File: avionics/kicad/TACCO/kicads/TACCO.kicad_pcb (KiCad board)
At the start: 6 copper layers, 55 x 35 mm, 143 parts, among them X2Y-CAN 4.7nF X2Y, X2Y-RS485 4.7nF X2Y

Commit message: feat(avionics): Phase 3 — TACCO HI-1573+PRU -> HI-6138 (MIL-STD-1553C)
gen_tacco_sch.py drift fixed first (pre-rename XO lib nickname/sym path,
stale TPS63031 datasheet text); regenerated output proven netlist-
identical to the committed schematic (0 comp / 0 pin-net diffs), ERC 0.
Then: 1553-XCVR -> HI-6138PCIF, X-50M/C-50M/R-1553IRQ/C-1553D, PB2
P1-7/8/9 -> M1553B_IRQN/MRN/TX_INH, P1-20 -> SPI0_B_CS_1553. TACCO's
_B_ net suffix kept (cape-B convention, not a 1553B label).

PCB patched in place. HI-6138 at the old site (142.86, 111.49, B.Cu).
No collision-free site within 20 mm on either side for the 4 new parts
(TACCO area crisis) -> parked off-board, owner placement item in WBS.
swap tool: NPTH now blocks the opposite side; courtyard margin 0.25 mm.

Gates: ERC 0; DRC 169 = pre-change baseline 169 (no new violations),
0 schematic parity; unconnected 480 -> 482.

Co-Authored-By: Claude Opus 5.5 <noreply@anthropic.com>
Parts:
- removed the 1553-XCVR at (142.9, 111.5)
- added 1553-XCVR: HI-6138PCIF, Serenity-Custom:Holt_HI-6138_QFN-48_6x6mm_P0.4mm_EP4.6mm, B.Cu at (142.9, 111.5)
- added C-1553D: 100nF, Capacitor_SMD:C_0402_1005Metric, B.Cu at (184.0, 92.5)
- added C-50M: 100nF, Capacitor_SMD:C_0402_1005Metric, B.Cu at (180.0, 92.5)
- added R-1553IRQ: 10k, Resistor_SMD:R_0402_1005Metric, B.Cu at (188.0, 92.5)
- added X-50M: 50MHz 3.3V, Oscillator:Oscillator_SMD_ECS_2520MV-xxx-xx-4Pin_2.5x2.0mm, B.Cu at (192.0, 92.5)
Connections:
- PB2-P1 pad 10: PRU_1553B_TX_P -> (no net)
- PB2-P1 pad 20: M1553B_TX_INH -> SPI0_B_CS_1553
- PB2-P1 pad 7: PRU_1553B_RX_N -> M1553B_IRQN
- PB2-P1 pad 8: PRU_1553B_RX_P -> M1553B_MRN
- PB2-P1 pad 9: PRU_1553B_TX_N -> M1553B_TX_INH

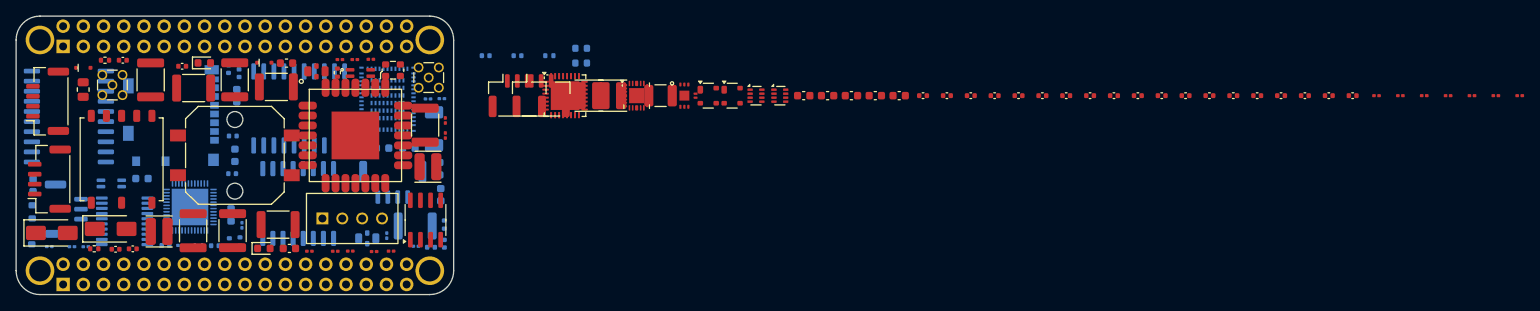
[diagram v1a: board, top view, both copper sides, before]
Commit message: feat(avionics): TACCO Rev S3 — area recovery, bare STM32WLE5JC mLRS radio, verified PB2 header map, DRC-clean placement
Owner decisions of 2026-09-29 (avionics/WBS.md §1.2a "TACCO area recovery"),
documented first per the design-shift gate, then implemented:

- Ferrite-bead spec defect: FB-SDIO1..6 / FB-WIOE5-1/2 carried Würth 742792510,
  which wurth-742792510.pdf shows is the 1812 5 A / 70 Ω power bead; the signal
  beads are now 0402 600 Ω positions (MPN owner-select). FB1 keeps 742792510.
- Boot/bind switch PTS125 -> C&K KMR2; SWD header JST-GH -> Tag-Connect
  TC2030-NL pads. Wi-Fi/TPM 100 nF bypasses -> 0201 (rail-cell sites).
- Seeed Wio-E5 (Chinese-built module) -> bare ST STM32WLE5JCU6 with Epson
  TG2520SMN 32 MHz TCXO and pSemi PE4259 antenna switch; pins from DS13105 Rev 9
  Fig. 9 / Table 19; SMPS Lout 15 µH / Cout 470 nF per DS13105; TCXO series 10 pF
  per Table 58. RF matching values are tagged VERIFY AN5457 (not obtainable here).
- PB2 P1/P2 header map rebuilt from the owner-supplied PocketBeagle 2 schematic
  (REF-SENSOR-021, avionics/kicad/PB2_HEADER_PINMAP.md): the Rev S2 map put GND on
  the PB2's 5 V VIN pin and peripherals on the wrong balls. MCAN0 on P2-5/7,
  UART2 = RS-485 with hardware DE, UART0 = mLRS, UART1 = BT, SPI0 + CS1, RMII2 +
  MDIO0 for Ethernet (RMII0_* -> RMII2_*), EHRPWM2_A = fan.
- MMC2/SDIO is not on the PB2 headers: Type 2EL WLAN cannot be hosted; SDIO beads
  deleted, module SDIO pins NC. Owner decision: Wi-Fi moves to a USB module on
  USB1 (P1-9/11) — module selection is an open fab blocker.
- DP83825I pin table rebuilt from TI SNLS638C Table 4-1 (REF-SENSOR-020); the old
  table was not this part's pinout (Pilot shares the defect, not fixed here).
  Pin 2 (50MHzOut) now drives RMII2_REF_CLK.
- Non-stack-through rails (Commo Rev T standalone): the placer may use the
  top-face cells between rail pins for 0201 parts. The P2-3..10 gap idea was
  withdrawn once the real map showed P2-5/7 are the only MCAN0 pins.
- gen_tacco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
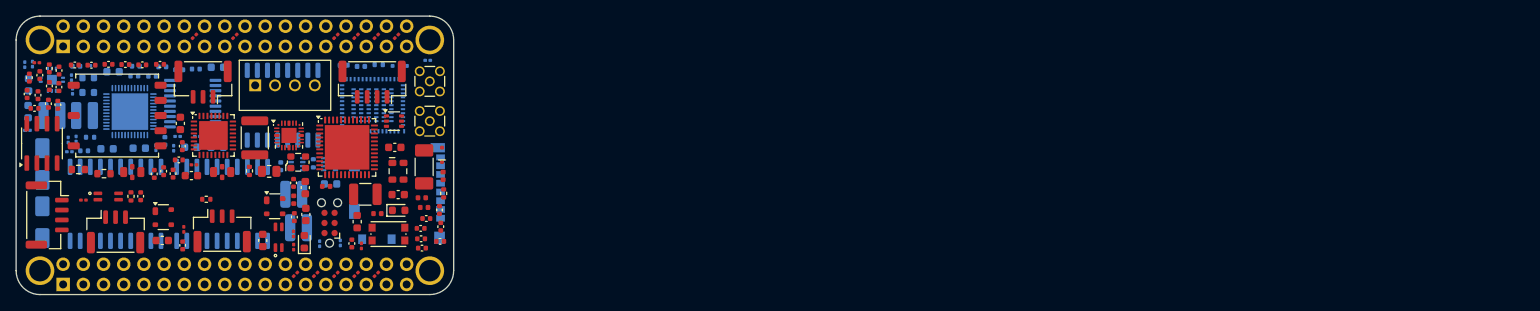
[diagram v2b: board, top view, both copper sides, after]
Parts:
- removed C-WIOE5-IN: 4.7uF, Capacitor_SMD:C_0603_1608Metric
- removed C-WIOE5-SH1, C-WIOE5-SH2: DNP, Capacitor_SMD:C_0201_0603Metric
- removed the C-ZB-SDVIO at (286.0, 97.5)
- removed the C-ZB-VIO at (289.0, 97.5)
- removed D-ANT-WIOE5: RCLAMP0502B, Serenity-Custom:RCLAMP0502B_SOD882
- removed FB-SDIO1, FB-SDIO2, FB-SDIO3, FB-SDIO4, FB-SDIO5, FB-SDIO6, FB-WIOE5-1, FB-WIOE5-2: 742792510, Inductor_SMD:L_1812_4532Metric
- removed J-ANT-WIOE5: MMCX vertical, Connector_Coaxial:MMCX_Molex_73415-1471_Vertical
- removed J-WIOE5-SWD: SM04B-GHS-TB, Connector_JST:JST_GH_SM04B-GHS-TB_1x04-1MP_P1.25mm_Horizontal
- removed L-WIOE5-SER: 0R link, Resistor_SMD:R_0402_1005Metric
- removed LED-WIOE5-G: Green, LED_SMD:LED_0603_1608Metric
- removed LED-WIOE5-R: Red, LED_SMD:LED_0603_1608Metric
- removed R-WIOE5-LEDG, R-WIOE5-LEDR: 1k, Resistor_SMD:R_0201_0603Metric
- removed R-WIOE5-RST: 22k, Resistor_SMD:R_0201_0603Metric
- removed R-WIOE5-SWCLK, R-WIOE5-SWDIO: 22R, Resistor_SMD:R_0201_0603Metric
- removed SW-WIOE5-BOOT: PTS125Sx43, Button_Switch_SMD:SW_Push_1P1T_NO_CK_PTS125Sx43PSMTR
- removed WIOE5: Wio-E5, Serenity-Custom:Seeed_WioE5_QFN28
- added C-MLRS-BULK: 4.7uF, Capacitor_SMD:C_0603_1608Metric, F.Cu at (168.6, 104.0)
- added C-MLRS-HSE: 10pF C0G, Capacitor_SMD:C_0402_1005Metric, F.Cu at (171.9, 114.2)
- added C-MLRS-RST: 100nF, Capacitor_SMD:C_0402_1005Metric, F.Cu at (171.9, 115.5)
- added C-MLRS-RX1: VERIFY AN5457, Capacitor_SMD:C_0402_1005Metric, F.Cu at (174.4, 114.0)
- added C-MLRS-RXN: VERIFY AN5457, Capacitor_SMD:C_0402_1005Metric, F.Cu at (174.3, 115.8)
- added C-MLRS-RXP: VERIFY AN5457, Capacitor_SMD:C_0402_1005Metric, F.Cu at (172.0, 116.7)
- added C-MLRS-SH1: DNP, Capacitor_SMD:C_0201_0603Metric, F.Cu at (164.4, 116.4)
- added C-MLRS-SH2: DNP, Capacitor_SMD:C_0201_0603Metric, F.Cu at (155.9, 114.9)
- added C-MLRS-SMPS: 100nF, Capacitor_SMD:C_0402_1005Metric, F.Cu at (139.5, 107.0)
- added C-MLRS-TCXO: 100nF, Capacitor_SMD:C_0402_1005Metric, F.Cu at (141.5, 105.6)
- added C-MLRS-TX0: VERIFY AN5457, Capacitor_SMD:C_0402_1005Metric, F.Cu at (155.9, 108.5)
- added C-MLRS-TX1: VERIFY AN5457, Capacitor_SMD:C_0402_1005Metric, F.Cu at (138.4, 107.3)
- added C-MLRS-TX2: VERIFY AN5457, Capacitor_SMD:C_0402_1005Metric, F.Cu at (139.1, 93.6)
- added C-MLRS-VBAT: 100nF, Capacitor_SMD:C_0402_1005Metric, F.Cu at (136.9, 93.6)
- added C-MLRS-VDD1: 100nF, Capacitor_SMD:C_0402_1005Metric, F.Cu at (134.7, 93.6)
- added C-MLRS-VDD2: 100nF, Capacitor_SMD:C_0402_1005Metric, F.Cu at (132.6, 93.6)
- added C-MLRS-VDDA1: 100nF, Capacitor_SMD:C_0402_1005Metric, F.Cu at (130.5, 93.7)
- added C-MLRS-VDDA2: 1uF, Capacitor_SMD:C_0402_1005Metric, F.Cu at (128.4, 93.6)
- added C-MLRS-VDDPA1: 100nF, Capacitor_SMD:C_0402_1005Metric, F.Cu at (126.2, 98.6)
- added C-MLRS-VDDPA2: 4.7uF, Capacitor_SMD:C_0603_1608Metric, F.Cu at (169.0, 109.9)
- added C-MLRS-VDDRF: 100nF, Capacitor_SMD:C_0402_1005Metric, F.Cu at (126.4, 96.4)
- added C-MLRS-VFB: 470nF, Capacitor_SMD:C_0402_1005Metric, F.Cu at (126.4, 94.3)
- added C-MLRS-VRPA: 100nF VERIFY AN5457, Capacitor_SMD:C_0402_1005Metric, B.Cu at (141.5, 94.2)
- added C-ZB-SDVIO: 100nF 6.3V X5R, Capacitor_SMD:C_0201_0603Metric, B.Cu at (127.5, 103.1)
- added C-ZB-VIO: 100nF 6.3V X5R, Capacitor_SMD:C_0201_0603Metric, F.Cu at (166.3, 90.0)
- added D-ANT-MLRS: RCLAMP0502B, Serenity-Custom:RCLAMP0502B_SOD882, F.Cu at (174.5, 104.9)
- added FB-MLRS-1: 600R@100MHz 0402, Inductor_SMD:L_0402_1005Metric, F.Cu at (160.0, 108.9)
- added FB-MLRS-2: 600R@100MHz 0402, Inductor_SMD:L_0402_1005Metric, F.Cu at (155.9, 110.6)
- added J-ANT-MLRS: MMCX vertical, Connector_Coaxial:MMCX_Molex_73415-1471_Vertical, F.Cu at (173.0, 100.7)
- added J-MLRS-SWD: TC2030-IDC-NL pads, Connector:Tag-Connect_TC2030-IDC-NL_2x03_P1.27mm_Vertical, F.Cu at (160.4, 113.5)
- added L-MLRS-PA: VERIFY AN5457, Inductor_SMD:L_0402_1005Metric, F.Cu at (166.4, 112.3)
- added L-MLRS-RX1: VERIFY AN5457, Inductor_SMD:L_0402_1005Metric, B.Cu at (164.3, 93.8)
- added L-MLRS-RX2: VERIFY AN5457, Inductor_SMD:L_0402_1005Metric, F.Cu at (174.7, 107.6)
- added L-MLRS-SER: 0R link, Resistor_SMD:R_0402_1005Metric, F.Cu at (174.7, 109.8)
- added L-MLRS-SMPS: 15uH, Inductor_SMD:L_0603_1608Metric, F.Cu at (163.9, 113.3)
- added L-MLRS-TX1: VERIFY AN5457, Inductor_SMD:L_0402_1005Metric, F.Cu at (172.0, 110.3)
- added L-MLRS-TX2: VERIFY AN5457, Inductor_SMD:L_0402_1005Metric, F.Cu at (172.3, 111.6)
- added LED-MLRS-G: Green, LED_SMD:LED_0603_1608Metric, F.Cu at (169.1, 111.9)
- added LED-MLRS-R: Red, LED_SMD:LED_0603_1608Metric, F.Cu at (157.2, 115.9)
- added MLRS-MCU: STM32WLE5JCU6, Package_DFN_QFN:QFN-48-1EP_7x7mm_P0.5mm_EP5.6x5.6mm, F.Cu at (162.6, 104.0)
- added R-MLRS-BOOT0: 10k, Resistor_SMD:R_0201_0603Metric, F.Cu at (163.7, 120.0)
- added R-MLRS-LEDG: 1k, Resistor_SMD:R_0201_0603Metric, F.Cu at (161.2, 90.0)
- added R-MLRS-LEDR: 1k, Resistor_SMD:R_0201_0603Metric, F.Cu at (156.1, 120.0)
- added R-MLRS-RST: 22k, Resistor_SMD:R_0201_0603Metric, F.Cu at (166.3, 120.0)
- added R-MLRS-SWCLK: 22R, Resistor_SMD:R_0201_0603Metric, F.Cu at (163.7, 90.0)
- added R-MLRS-SWDIO: 22R, Resistor_SMD:R_0201_0603Metric, F.Cu at (168.8, 90.0)
- added RFSW-MLRS: PE4259, Package_TO_SOT_SMD:SOT-363_SC-70-6, F.Cu at (168.5, 100.7)
- added SW-MLRS: KMR2 tact, Button_Switch_SMD:SW_Push_1P1T_NO_CK_KMR2, F.Cu at (167.8, 114.9)
- added X-MLRS: TG2520SMN 32MHz 1.8V clipped-sine, Oscillator:Oscillator_SMD_SeikoEpson_TG2520SMN-xxx-xxxxxx-4Pin_2.5x2.0mm, F.Cu at (169.0, 107.0)
- C-1V8RF-IN, C-25M, C-3V3-HF, C-3V3-IN, C-3V3-O1, C-3V3-O2, C-BST, C-CAN1, C-PLD1, C-RF-IN2, C-RF-O2, C-SS, C-SS18, D-ANT-RADIO, L-1V8RF, L-3V3, L-ANT-SER, L-RF1, L-RF2, R-AD0, R-EN3, R-FB3H, R-FB3L, R-RBIAS, TVS-1553N, TVS-1553P, U-1V8RF, U-3V3, U-3V3RF: moved to B.Cu
- C-1V8RF-O1, C-1V8RF-O2, C-485-2, C-485-3, C-485-4, C-485-5, C-485-6, C-BS, C-BST18, C-CAN6, C-FLASH1, C-PHY-A2, CMC-RS485, J-485, J-ETH, R-1553N, R-1553P, R-BST, R-CANT, R-TPMCS, X2Y-RS485: moved to F.Cu
- C-TPM2, C-TPM3, C-ZB-18-2, C-ZB-33-1, C-ZB-33-2: value 100nF -> 100nF 6.3V X5R; footprint Capacitor_SMD:C_0402_1005Metric -> Capacitor_SMD:C_0201_0603Metric; moved to B.Cu
- C-TPM4, C-ZB-18-1: value 100nF -> 100nF 6.3V X5R; footprint Capacitor_SMD:C_0402_1005Metric -> Capacitor_SMD:C_0201_0603Metric
- moved R-FB3L 181.0 mm to (123.1, 93.5), turned to 90 degrees
- moved R-EN3 170.1 mm to (128.0, 95.2), turned to 90 degrees
- moved C-ZB-33-2 154.9 mm to (128.1, 96.9), turned to 90 degrees
- moved R-FB18L 153.0 mm to (158.7, 120.0), turned to 45 degrees
- moved C-ZB-33-1 151.6 mm to (128.5, 102.9), turned to 90 degrees
- moved C-SS18 151.3 mm to (143.8, 102.6)
- moved C-TPM4 150.4 mm to (123.6, 93.4)
- moved R-FB18H 147.5 mm to (161.2, 120.0), turned to 45 degrees
- moved C-ZB-18-2 146.4 mm to (130.7, 93.7)
- moved R-FB3H 143.1 mm to (159.2, 116.1), turned to 90 degrees
- moved C-TPM1 142.4 mm to (122.7, 95.2), turned to 90 degrees
- moved C-PHY-CTD2 133.6 mm to (122.4, 97.3), turned to 90 degrees
- moved C-RF-IN2 133.5 mm to (128.6, 93.8)
- moved C-SS 131.6 mm to (161.8, 116.0), turned to 90 degrees
- moved C-TPM3 130.4 mm to (140.8, 104.1), turned to 90 degrees
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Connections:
- ETH-PHY pad 1: RMII0_RXD0 -> RMII2_TX_EN
- ETH-PHY pad 10: GND -> ETHB_TXN
- ETH-PHY pad 11: (no net) -> ETHB_TXP
- ETH-PHY pad 12: PHY1_RSTN -> (no net)
- ETH-PHY pad 13: MDIO0 -> PHY_XI_25M
- ETH-PHY pad 14: MDC0 -> ETH-PHY_RBIAS
- ETH-PHY pad 15: PHY1_INTRN -> MDIO0
- ETH-PHY pad 16: GND -> MDC0
- ETH-PHY pad 17: ETHB_TXP -> RMII2_RXD1
- ETH-PHY pad 18: ETHB_TXN -> RMII2_RXD0
- ETH-PHY pad 2: RMII0_RXD1 -> RMII2_REF_CLK
- ETH-PHY pad 20: GND -> RMII2_CRS_DV
- ETH-PHY pad 21: ETHB_RXP -> GND
- ETH-PHY pad 22: ETHB_RXN -> RMII2_RX_ER
- ETH-PHY pad 23: +3V3 -> RMII2_TXD0
- ETH-PHY pad 24: ETH-PHY_RBIAS -> RMII2_TXD1
- ETH-PHY pad 3: RMII0_RX_ER -> PHY1_INTRN
- ETH-PHY pad 4: RMII0_CRS_DV -> (no net)
- ETH-PHY pad 5: RMII0_TX_EN -> PHY1_RSTN
- ETH-PHY pad 6: RMII0_TXD0 -> +3V3
- ETH-PHY pad 7: RMII0_TXD1 -> ETHB_RXN
- ETH-PHY pad 8: PHY_XI_25M -> ETHB_RXP
- ETH-PHY pad 9: (no net) -> GND
- PB2-P1 pad 1: GND -> +5V
- PB2-P1 pad 10: (no net) -> BT_UART_CTS
- PB2-P1 pad 11: RS485_B_DE -> (no net)
- PB2-P1 pad 12: RS485_B_RX -> BT_UART_RTS
- PB2-P1 pad 13: RS485_B_TX -> PLD_CLK
- PB2-P1 pad 14: CAN_B_STB -> +3V3_PB2
- PB2-P1 pad 15: MCAN0_B_RX -> GND
- PB2-P1 pad 16: MCAN0_B_TX -> GND
- PB2-P1 pad 17: SD_CD -> (no net)
- PB2-P1 pad 19: (no net) -> RMII2_RX_ER
- PB2-P1 pad 2: GND -> RMII2_TX_EN
- PB2-P1 pad 20: SPI0_B_CS_1553 -> PLD_I1
- PB2-P1 pad 21: SPI0_B_CS_TPM -> PLD_I2
- PB2-P1 pad 22: SPI0_B_CS_FLASH -> GND
- PB2-P1 pad 23: SPI0_B_MISO -> PLD_I3
- PB2-P1 pad 24: SPI0_B_MOSI -> (no net)
- PB2-P1 pad 25: SPI0_B_CLK -> RMII2_RXD1
- PB2-P1 pad 26: SPI0_B_CS_ZB -> PLD_I4
- PB2-P1 pad 27: ZB_SPI_INT -> RMII2_RXD0
- PB2-P1 pad 28: (no net) -> PLD_I5
- PB2-P1 pad 29: (no net) -> PLD_I6
- PB2-P1 pad 3: BT_UART_TX -> (no net)
- PB2-P1 pad 30: (no net) -> UART_WIOE5_TX
- PB2-P1 pad 31: UART_WIOE5_RX -> PLD_I7
- PB2-P1 pad 32: UART_WIOE5_TX -> UART_WIOE5_RX
- PB2-P1 pad 33: +3V3_PB2 -> PLD_I8
- PB2-P1 pad 34: +3V3_PB2 -> RMII2_REF_CLK
- PB2-P1 pad 35: +5V -> RMII2_CRS_DV
- PB2-P1 pad 36: GND -> FAN_PWM_B
- PB2-P1 pad 4: BT_UART_RX -> RMII2_TXD0
- PB2-P1 pad 5: BT_UART_RTS -> (no net)
- PB2-P1 pad 6: BT_UART_CTS -> BT_UART_RX
- PB2-P1 pad 7: M1553B_IRQN -> +5V
- PB2-P1 pad 8: M1553B_MRN -> BT_UART_TX
- PB2-P1 pad 9: M1553B_TX_INH -> (no net)
- PB2-P2 pad 1: SDIO_D2 -> MDC0
- PB2-P2 pad 10: WIFI_IRQ -> M1553B_MRN
- PB2-P2 pad 11: TPM_B_RSTN -> RS485_B_TX
- PB2-P2 pad 12: TPM_B_IRQN -> (no net)
- PB2-P2 pad 13: PLD_I3 -> (no net)
- PB2-P2 pad 14: PLD_I4 -> (no net)
- PB2-P2 pad 15: PHY1_RSTN -> GND
- PB2-P2 pad 16: PHY1_INTRN -> (no net)
- PB2-P2 pad 17: MDIO0 -> M1553B_TX_INH
- PB2-P2 pad 18: MDC0 -> TPM_B_RSTN
- PB2-P2 pad 19: SDIO_CLK -> TPM_B_IRQN
- PB2-P2 pad 2: SDIO_D3 -> CAN_B_STB
- PB2-P2 pad 20: SDIO_CMD -> SD_CD
- PB2-P2 pad 21: SDIO_D0 -> GND
- PB2-P2 pad 22: SDIO_D1 -> RS485_B_DE
- PB2-P2 pad 23: PLD_I5 -> +3V3_PB2
- PB2-P2 pad 24: PLD_I6 -> SPI0_B_CS_1553
- PB2-P2 pad 25: PLD_I7 -> SPI0_B_MOSI
- PB2-P2 pad 26: PLD_I8 -> (no net)
- PB2-P2 pad 27: (no net) -> SPI0_B_MISO
- PB2-P2 pad 28: RMII0_RX_ER -> WIFI_EN
- PB2-P2 pad 29: RMII0_CRS_DV -> SPI0_B_CLK
- PB2-P2 pad 3: (no net) -> MDIO0
- PB2-P2 pad 30: RMII0_RXD1 -> SPI0_B_CS_FLASH
- PB2-P2 pad 31: RMII0_RXD0 -> RMII2_TXD1
- PB2-P2 pad 32: RMII0_TX_EN -> SPI0_B_CS_ZB
- PB2-P2 pad 33: RMII0_TXD1 -> WIFI_IRQ
- PB2-P2 pad 34: RMII0_TXD0 -> ZB_SPI_INT
- PB2-P2 pad 35: +5V -> (no net)
- PB2-P2 pad 36: GND -> SPI0_B_CS_TPM
- PB2-P2 pad 4: (no net) -> PHY1_RSTN
- PB2-P2 pad 5: FAN_PWM_B -> MCAN0_B_TX
- PB2-P2 pad 6: PLD_CLK -> PHY1_INTRN
- PB2-P2 pad 7: PLD_I1 -> MCAN0_B_RX
- PB2-P2 pad 8: PLD_I2 -> M1553B_IRQN
- PB2-P2 pad 9: WIFI_EN -> RS485_B_RX
- R-AD0 pad 2: RMII0_RXD0 -> RMII2_RXD0
- WIFI-BT-ZB pad 42: SDIO_CMD_F -> (no net)
- WIFI-BT-ZB pad 44: SDIO_CLK_F -> (no net)
- WIFI-BT-ZB pad 45: SDIO_D1_F -> (no net)
- WIFI-BT-ZB pad 46: SDIO_D3_F -> (no net)
- WIFI-BT-ZB pad 47: SDIO_D2_F -> (no net)
- WIFI-BT-ZB pad 48: SDIO_D0_F -> (no net)
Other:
- board text added: "TACCO Rev S3 Griffing Technology LLC CC BY 4.0"
- board text removed: "XO Rev S2 Griffing Technology LLC CC BY 4.0"

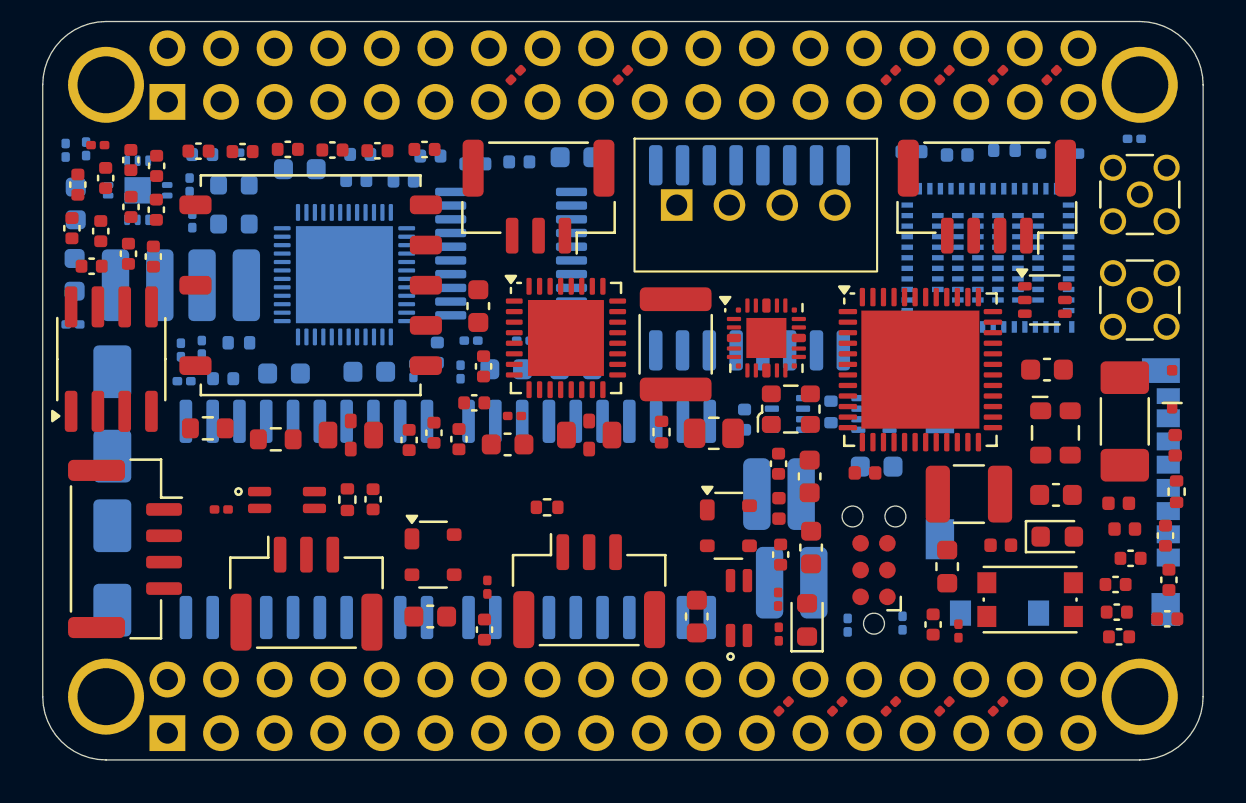
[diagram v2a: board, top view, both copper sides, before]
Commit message: feat(avionics): TACCO routing prep — 0.6 mm vias, plane fanout, QFN thermal vias, edge/band keepouts for the Specctra bridge
- Netclass vias 0.6/0.3 mm so hole-to-copper stays >= 0.25 mm at the 0.127 mm
  clearance freerouting works to (phase-1 trial produced 199 hole-clearance
  errors with 0.5 mm vias).
- finish_tacco_pcb.py: 'prepare' step places the STM32WLE5JC exposed-pad thermal
  vias and a GND/+3V3 plane fanout (via + stub per SMD pad where the site is
  free, outside the isolation band, DRC-verified) before routing; 'export' adds a
  copper-to-edge keepout ring next to the band keepouts; gerber export script.
- Board committed in the prepared state: 0 DRC errors, 0 parity issues, 499
  unconnected (routing in progress).

Co-Authored-By: Claude Fable 5.1 <noreply@anthropic.com>
Claude-Session: https://claude.ai/code/session_01YLwDy53g1VCBzNBwW4moUC
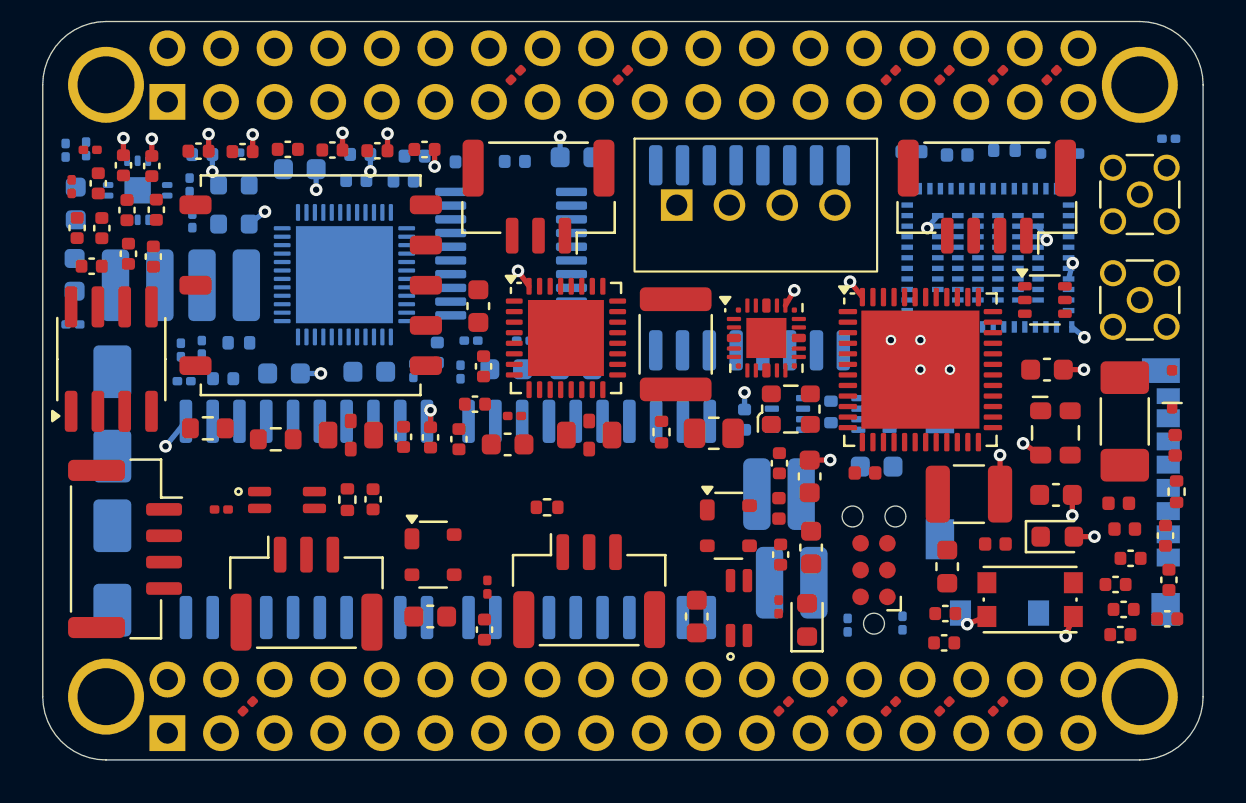
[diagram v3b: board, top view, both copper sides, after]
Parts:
- C-BST18, C-MLRS-SH2: moved to B.Cu
- C-MLRS-VRPA, R-AD0: moved to F.Cu
- moved R-AD0 40.3 mm to (122.4, 95.3)
- moved C-MLRS-TCXO 32.3 mm to (172.2, 115.4)
- moved C-BST18 31.2 mm to (141.0, 94.2), turned to 0 degrees
- moved C-MLRS-SMPS 26.2 mm to (163.7, 117.0), turned to 0 degrees
- moved R-FLASH-WP 25.4 mm to (130.7, 120.0), turned to 45 degrees
- moved C-MLRS-VFB 18.8 mm to (141.5, 105.6), turned to 0 degrees
- moved C-MLRS-TX0 18.1 mm to (172.1, 116.6), turned to 0 degrees
- moved C-MLRS-RXP 18.1 mm to (155.9, 108.4), turned to 90 degrees
- moved C-MLRS-VRPA 13.4 mm to (138.1, 107.2), turned to 90 degrees
- moved C-MLRS-SH2 12.5 mm to (161.7, 103.8)
- moved C-MLRS-SH1 8.60 mm to (155.9, 115.2)
- moved C-MLRS-RST 8.13 mm to (163.8, 115.6)
- moved C-PHY-A2 4.30 mm to (126.2, 94.3)
- moved C-PHY-CTD1 3.30 mm to (124.8, 94.3)
- moved C-PHY-CTD2 2.47 mm to (123.6, 95.2)
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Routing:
- net GND: track 0.00 -> 24.5 mm, vias 0 -> 31
- net +3V3: track 0.00 -> 4.29 mm, vias 0 -> 4
